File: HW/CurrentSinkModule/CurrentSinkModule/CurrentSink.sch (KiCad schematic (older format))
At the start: 103 parts, among them J1 Conn_01x03, J2 Conn_01x03, U1 LTC2058, U2 LTC2058, U3 LTC2058, U4 LTC2058

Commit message: updated
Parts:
- removed Q_NEGMOS1: IRF5210, Package_TO_SOT_THT:TO-220-3_Vertical, symbol Transistor_FET:IRF4905
- removed Q_POSMOS1: IRF3710, Package_TO_SOT_THT:TO-220-3_Vertical, symbol Transistor_FET:IRF3205
- added J3, J4: MosfetSocketx3, TerminalBlock:TerminalBlock_bornier-3_P5.08mm, symbol MosfetSocket:MosfetSocketx3
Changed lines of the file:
@@
 	1    0    0    -1
 $EndComp
-$Comp
-L Transistor_FET:IRF3205 Q_POSMOS1
-U 1 1 5C970D9A
-P 14300 4650
-F 0 "Q_POSMOS1" H 14506 4695 50  0000 L CNN
-F 1 "IRF3710" H 14506 4606 50  0000 L CNN
-F 2 "Package_TO_SOT_THT:TO-220-3_Vertical" H 14550 4575 50  0001 L CIN
-F 3 "https://www.mouser.co.uk/datasheet/2/196/irf3710pbf-1227029.pdf" H 14300 4650 50  0001 L CNN
-F 4 "942-IRF3710PBF" H 14300 4650 50  0001 C CNN "MouserNo"
-	1    14300 4650
-	1    0    0    -1
-$EndComp
-$Comp
-L Transistor_FET:IRF4905 Q_NEGMOS1
-U 1 1 5C970DA3
-P 14300 15925
-F 0 "Q_NEGMOS1" H 14506 15970 50  0000 L CNN
-F 1 "IRF5210" H 14506 15881 50  0000 L CNN
-F 2 "Package_TO_SOT_THT:TO-220-3_Vertical" H 14500 15850 50  0001 L CIN
-F 3 "https://www.mouser.co.uk/datasheet/2/196/irf5210pbf-1228304.pdf" H 14300 15925 50  0001 L CNN
-F 4 "942-IRF5210PBF" H 14300 15925 50  0001 C CNN "MouserNo"
-F 5 "942-IRF4905PBF" H 14300 15925 50  0001 C CNN "Mfr. No:"
-	1    14300 15925
-	1    0    0    1
-$EndComp
-Wire Wire Line
-	14400 3850 14400 4450
 Wire Wire Line
 	10400 4750 10400 5600
@@
 Wire Wire Line
 	5450 15400 5650 15400
-Wire Wire Line
-	14400 4850 14400 5600
 $Comp
 L Device:R R24
@@
 Wire Wire Line
 	13800 4000 13800 4650
-Wire Wire Line
-	13800 4650 14100 4650
 $Comp
 L Connector:TestPoint TP5
@@
 Connection ~ 12800 15925
 Wire Wire Line
-	12800 15925 14100 15925
+	12800 15925 14400 15925
 Wire Wire Line
 	6600 6400 7600 6400
@@
 	14400 14400 14400 15325
 Wire Wire Line
-	14400 15325 14400 15725
+	14400 15325 14400 15825
 Connection ~ 14400 15325
 Wire Wire Line
-	14400 16125 14400 17200
+	14400 16025 14400 17200
 Wire Wire Line
 	3650 20300 3650 20400
@@
 	0    1    1    0
 $EndComp
+Wire Wire Line
+	13800 4650 14400 4650
+Wire Wire Line
+	14400 4750 14400 5600
+Wire Wire Line
+	14400 3850 14400 4550
+$Comp
+L MosfetSocket:MosfetSocketx3 J3
+U 1 1 5D3BDBA1
+P 14600 4650
+F 0 "J3" H 14680 4692 50  0000 L CNN
+F 1 "MosfetSocketx3" H 14680 4601 50  0000 L CNN
+F 2 "TerminalBlock:TerminalBlock_bornier-3_P5.08mm" H 14600 4650 50  0001 C CNN
+F 3 "https://docs-emea.rs-online.com/webdocs/0130/0900766b8013040c.pdf" H 14600 4650 50  0001 C CNN
+	1    14600 4650
+	1    0    0    -1
+$EndComp
+$Comp
+L MosfetSocket:MosfetSocketx3 J4
+U 1 1 5D4094FF
+P 14600 15925
+F 0 "J4" H 14518 15600 50  0000 C CNN
+F 1 "MosfetSocketx3" H 14518 15691 50  0000 C CNN
+F 2 "TerminalBlock:TerminalBlock_bornier-3_P5.08mm" H 14600 15925 50  0001 C CNN
+F 3 "https://docs-emea.rs-online.com/webdocs/0130/0900766b8013040c.pdf" H 14600 15925 50  0001 C CNN
+	1    14600 15925
+	1    0    0    1
+$EndComp
 $EndSCHEMATC

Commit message: Updates
- New simplified current sink design: see LTSpice model "MOSFET_CurrentSense_NoSignalInversion".
Needs to be confirmed on breadboard!
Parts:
- U1, U2, U3, U4: MouserNo ADA4522-2ARZ-RL -> LTC2058
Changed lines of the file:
@@
 Connection ~ 23150 14200
-$Comp
-L Amplifier_Operational:TL072 U2
-U 1 1 5E1E06F5
-P 5700 6400
-F 0 "U2" H 5700 6767 50  0000 C CNN
-F 1 "LTC2058" H 5700 6676 50  0000 C CNN
-F 2 "Package_SO:SOIC-8_3.9x4.9mm_P1.27mm" H 5700 6400 50  0001 C CNN
-F 3 "https://www.analog.com/media/en/technical-documentation/data-sheets/ADA4522-1_4522-2_4522-4.pdf" H 5700 6400 50  0001 C CNN
-F 4 "ADA4522-2ARZ-RL" H 5700 6400 50  0001 C CNN "MouserNo"
-	1    5700 6400
-	1    0    0    -1
-$EndComp
-$Comp
-L Amplifier_Operational:TL072 U2
-U 2 1 5E1E086A
-P 8200 6500
-F 0 "U2" H 8200 6867 50  0000 C CNN
-F 1 "LTC2058" H 8200 6776 50  0000 C CNN
-F 2 "Package_SO:SOIC-8_3.9x4.9mm_P1.27mm" H 8200 6500 50  0001 C CNN
-F 3 "https://www.analog.com/media/en/technical-documentation/data-sheets/ADA4522-1_4522-2_4522-4.pdf" H 8200 6500 50  0001 C CNN
-F 4 "ADA4522-2ARZ-RL" H 8200 6500 50  0001 C CNN "MouserNo"
-	2    8200 6500
-	1    0    0    -1
-$EndComp
 $Comp
 L Amplifier_Operational:TL072 U1
@@
 F 4 "584-ADA4522-2ARMZ" H 19075 20125 50  0001 C CNN "MouserNo"
 	3    19075 20125
-	1    0    0    -1
-$EndComp
-$Comp
-L Amplifier_Operational:TL072 U1
-U 1 1 5E1E25D3
-P 5950 15300
-F 0 "U1" H 5950 15667 50  0000 C CNN
-F 1 "LTC2058" H 5950 15576 50  0000 C CNN
-F 2 "Package_SO:SOIC-8_3.9x4.9mm_P1.27mm" H 5950 15300 50  0001 C CNN
-F 3 "https://www.analog.com/media/en/technical-documentation/data-sheets/ADA4522-1_4522-2_4522-4.pdf" H 5950 15300 50  0001 C CNN
-F 4 "ADA4522-2ARZ-RL" H 5950 15300 50  0001 C CNN "MouserNo"
-	1    5950 15300
-	1    0    0    -1
-$EndComp
-$Comp
-L Amplifier_Operational:TL072 U4
-U 2 1 5E1E2914
-P 11750 15925
-F 0 "U4" H 11750 16292 50  0000 C CNN
-F 1 "LTC2058" H 11750 16201 50  0000 C CNN
-F 2 "Package_SO:SOIC-8_3.9x4.9mm_P1.27mm" H 11750 15925 50  0001 C CNN
-F 3 "https://www.analog.com/media/en/technical-documentation/data-sheets/ADA4522-1_4522-2_4522-4.pdf" H 11750 15925 50  0001 C CNN
-F 4 "ADA4522-2ARZ-RL" H 11750 15925 50  0001 C CNN "MouserNo"
-	2    11750 15925
 	1    0    0    -1
 $EndComp
@@
 Wire Wire Line
 	10300 3900 10300 6500
-$Comp
-L Amplifier_Operational:TL072 U3
-U 1 1 5D881F19
-P 12250 4650
-F 0 "U3" H 12250 5017 50  0000 C CNN
-F 1 "LTC2058" H 12250 4926 50  0000 C CNN
-F 2 "Package_SO:SOIC-8_3.9x4.9mm_P1.27mm" H 12250 4650 50  0001 C CNN
-F 3 "https://www.analog.com/media/en/technical-documentation/data-sheets/ADA4522-1_4522-2_4522-4.pdf" H 12250 4650 50  0001 C CNN
-F 4 "ADA4522-2ARZ-RL" H 12250 4650 50  0001 C CNN "MouserNo"
-	1    12250 4650
-	1    0    0    -1
-$EndComp
 Wire Wire Line
 	11950 4550 10400 4550
@@
 F 1 "LTC2058" H 24800 14576 50  0000 C CNN
 F 2 "Package_SO:SOIC-8_3.9x4.9mm_P1.27mm" H 24800 14300 50  0001 C CNN
-F 3 "https://www.analog.com/media/en/technical-documentation/data-sheets/ADA4522-1_4522-2_4522-4.pdf" H 24800 14300 50  0001 C CNN
-F 4 "ADA4522-2ARZ-RL" H 24800 14300 50  0001 C CNN "MouserNo"
+F 3 "https://www.analog.com/media/en/technical-documentation/data-sheets/LTC2058.pdf" H 24800 14300 50  0001 C CNN
+F 4 "LTC2058" H 24800 14300 50  0001 C CNN "MouserNo"
 	1    24800 14300
 	1    0    0    1
@@
 	25650 14300 25100 14300
 Connection ~ 25650 14300
-$Comp
-L Amplifier_Operational:TL072 U1
-U 2 1 5DB4E8F2
-P 7950 15400
-F 0 "U1" H 7950 15767 50  0000 C CNN
-F 1 "LTC2058" H 7950 15676 50  0000 C CNN
-F 2 "Package_SO:SOIC-8_3.9x4.9mm_P1.27mm" H 7950 15400 50  0001 C CNN
-F 3 "https://www.analog.com/media/en/technical-documentation/data-sheets/ADA4522-1_4522-2_4522-4.pdf" H 7950 15400 50  0001 C CNN
-F 4 "ADA4522-2ARZ-RL" H 7950 15400 50  0001 C CNN "MouserNo"
-	2    7950 15400
-	1    0    0    -1
-$EndComp
 Wire Wire Line
 	6800 15300 7350 15300
@@
 F 1 "LTC2058" H 24450 7526 50  0000 C CNN
 F 2 "Package_SO:SOIC-8_3.9x4.9mm_P1.27mm" H 24450 7250 50  0001 C CNN
-F 3 "https://www.analog.com/media/en/technical-documentation/data-sheets/ADA4522-1_4522-2_4522-4.pdf" H 24450 7250 50  0001 C CNN
-F 4 "ADA4522-2ARZ-RL" H 24450 7250 50  0001 C CNN "MouserNo"
+F 3 "https://www.analog.com/media/en/technical-documentation/data-sheets/LTC2058.pdf" H 24450 7250 50  0001 C CNN
+F 4 "LTC2058" H 24450 7250 50  0001 C CNN "MouserNo"
 	2    24450 7250
 	1    0    0    -1
@@
 	1    0    0    1
 $EndComp
+$Comp
+L Amplifier_Operational:TL072 U3
+U 1 1 5D881F19
+P 12250 4650
+F 0 "U3" H 12250 5017 50  0000 C CNN
+F 1 "LTC2058" H 12250 4926 50  0000 C CNN
+F 2 "Package_SO:SOIC-8_3.9x4.9mm_P1.27mm" H 12250 4650 50  0001 C CNN
+F 3 "https://www.analog.com/media/en/technical-documentation/data-sheets/LTC2058.pdf" H 12250 4650 50  0001 C CNN
+F 4 "LTC2058" H 12250 4650 50  0001 C CNN "MouserNo"
+	1    12250 4650
+	1    0    0    -1
+$EndComp
+$Comp
+L Amplifier_Operational:TL072 U2
+U 2 1 5E1E086A
+P 8200 6500
+F 0 "U2" H 8200 6867 50  0000 C CNN
+F 1 "LTC2058" H 8200 6776 50  0000 C CNN
+F 2 "Package_SO:SOIC-8_3.9x4.9mm_P1.27mm" H 8200 6500 50  0001 C CNN
+F 3 "https://www.analog.com/media/en/technical-documentation/data-sheets/LTC2058.pdf" H 8200 6500 50  0001 C CNN
+F 4 "LTC2058" H 8200 6500 50  0001 C CNN "MouserNo"
+	2    8200 6500
+	1    0    0    -1
+$EndComp
+$Comp
+L Amplifier_Operational:TL072 U2
+U 1 1 5E1E06F5
+P 5700 6400
+F 0 "U2" H 5700 6767 50  0000 C CNN
+F 1 "LTC2058" H 5700 6676 50  0000 C CNN
+F 2 "Package_SO:SOIC-8_3.9x4.9mm_P1.27mm" H 5700 6400 50  0001 C CNN
+F 3 "https://www.analog.com/media/en/technical-documentation/data-sheets/LTC2058.pdf" H 5700 6400 50  0001 C CNN
+F 4 "LTC2058" H 5700 6400 50  0001 C CNN "MouserNo"
+	1    5700 6400
+	1    0    0    -1
+$EndComp
+$Comp
+L Amplifier_Operational:TL072 U1
+U 2 1 5DB4E8F2
+P 7950 15400
+F 0 "U1" H 7950 15767 50  0000 C CNN
+F 1 "LTC2058" H 7950 15676 50  0000 C CNN
+F 2 "Package_SO:SOIC-8_3.9x4.9mm_P1.27mm" H 7950 15400 50  0001 C CNN
+F 3 "https://www.analog.com/media/en/technical-documentation/data-sheets/LTC2058.pdf" H 7950 15400 50  0001 C CNN
+F 4 "LTC2058" H 7950 15400 50  0001 C CNN "MouserNo"
+	2    7950 15400
+	1    0    0    -1
+$EndComp
+$Comp
+L Amplifier_Operational:TL072 U1
+U 1 1 5E1E25D3
+P 5950 15300
+F 0 "U1" H 5950 15667 50  0000 C CNN
+F 1 "LTC2058" H 5950 15576 50  0000 C CNN
+F 2 "Package_SO:SOIC-8_3.9x4.9mm_P1.27mm" H 5950 15300 50  0001 C CNN
+F 3 "https://www.analog.com/media/en/technical-documentation/data-sheets/LTC2058.pdf" H 5950 15300 50  0001 C CNN
+F 4 "LTC2058" H 5950 15300 50  0001 C CNN "MouserNo"
+	1    5950 15300
+	1    0    0    -1
+$EndComp
+$Comp
+L Amplifier_Operational:TL072 U4
+U 2 1 5E1E2914
+P 11750 15925
+F 0 "U4" H 11750 16292 50  0000 C CNN
+F 1 "LTC2058" H 11750 16201 50  0000 C CNN
+F 2 "Package_SO:SOIC-8_3.9x4.9mm_P1.27mm" H 11750 15925 50  0001 C CNN
+F 3 "https://www.analog.com/media/en/technical-documentation/data-sheets/LTC2058.pdf" H 11750 15925 50  0001 C CNN
+F 4 "LTC2058" H 11750 15925 50  0001 C CNN "MouserNo"
+	2    11750 15925
+	1    0    0    -1
+$EndComp
 $EndSCHEMATC

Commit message: updated
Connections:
- net GNDS: now also R5.1; no longer R8.1
- net at C3.1, JP5.2, R19.1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: now also R7.1; no longer JP7.1, U1.5 (+)
- net at C4.1, JP6.2, R20.1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: now also R25.1; no longer JP8.1, U2.5 (+)
- net at J2.1 (Pin_1), JP8.2, U2.7: now also R6.1; no longer R25.2
- net at R6.2, U2.6 (-): now also JP8.1
- net at J1.1 (Pin_1), R8.2: now also JP7.2, U1.7; no longer R5.1, R7.1
- net at R5.2: now also U1.5 (+); no longer U1.6 (-)
- net +5V renamed +12V
- net +5VA renamed +12VA
- net -5V renamed -12V
- net -5VA renamed -12VA
- new net: R25.2, R26.2, U2.5 (+)
- new net: JP7.1, R7.2, R8.1, U1.6 (-)
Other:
- moved on the sheet: JP7, JP8, R23, R25, R26, R5, R6, R7, R8, U1B, U2B

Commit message: Finished CurrentSinkRevC layout
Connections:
- net +12VA is gone; now on net +12V: C21.2, C25.1, C31.1, C33.1, C5.1, C7.1, U1.8 (V+), U4.8 (V+), U_NEGIA1.7 (Vs+)
- net -12VA is gone; now on net -12V: C22.2, C26.1, C32.1, C34.1, C6.1, C8.1, U1.4 (V-), U4.4 (V-), U_NEGIA1.4 (Vs-)
- net ADCSIG2: now also U4.7; no longer U4.1
- net at J4.1 (Pin_1), TP5.1: now also U4.1; no longer U4.7
- net at R21.2: now also U4.2 (-); no longer U4.5 (+)
- net at R22.1: now also U4.5 (+); no longer U4.3 (+)
- net at R13.1, R16.1: now also U4.6 (-); no longer U4.2 (-)
- net at J1.2 (Pin_2): now also U4.3 (+); no longer U4.6 (-)
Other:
- moved on the sheet: U4A, U4B

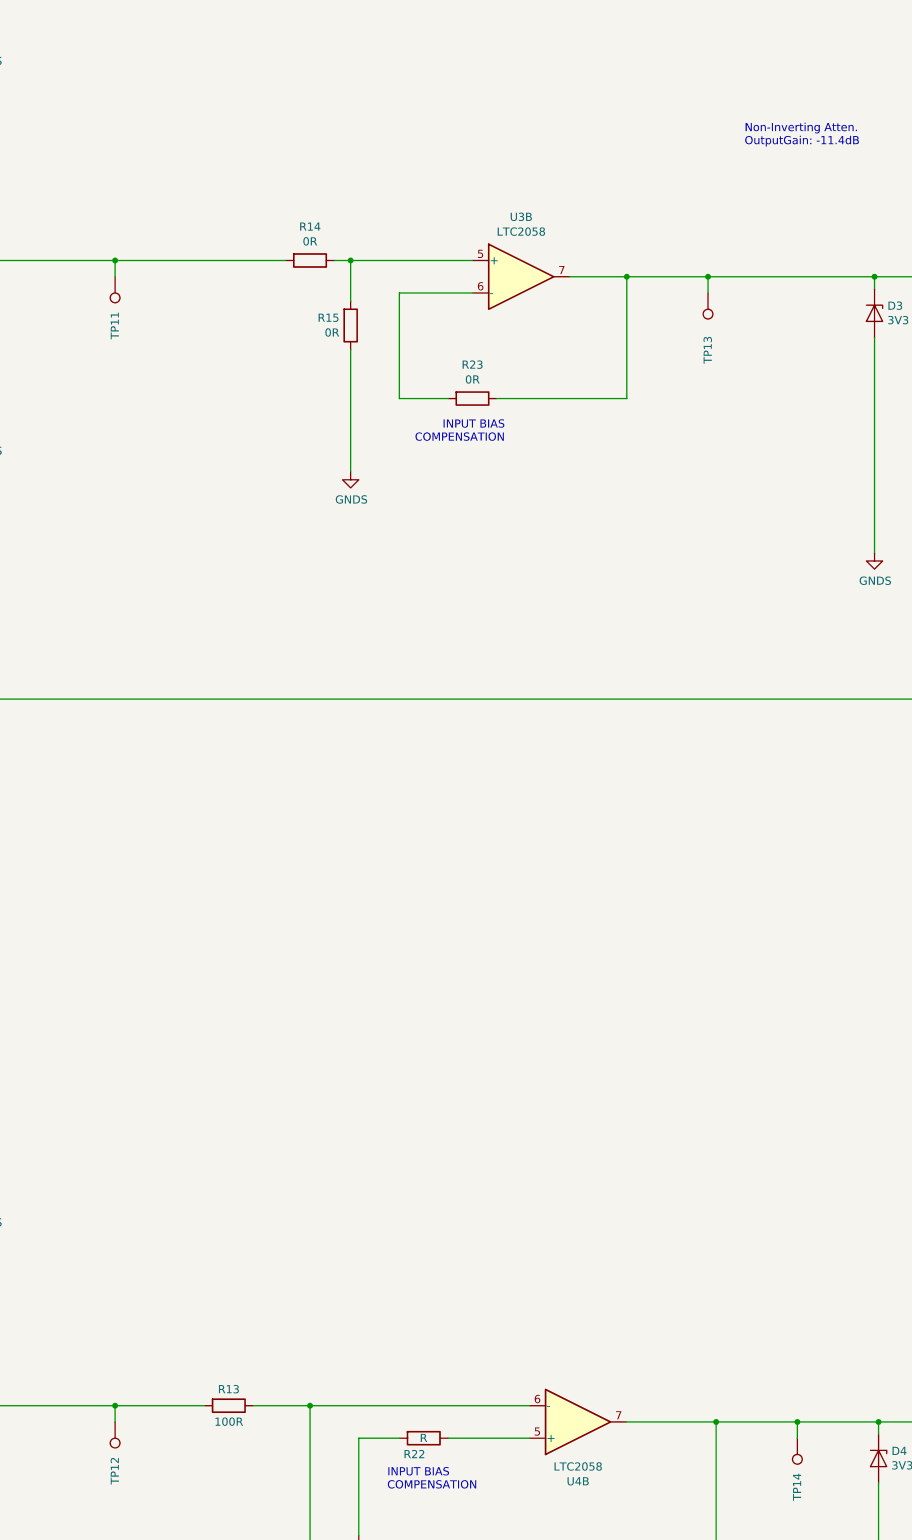
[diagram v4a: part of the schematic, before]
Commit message: Added Interafec IBOMS
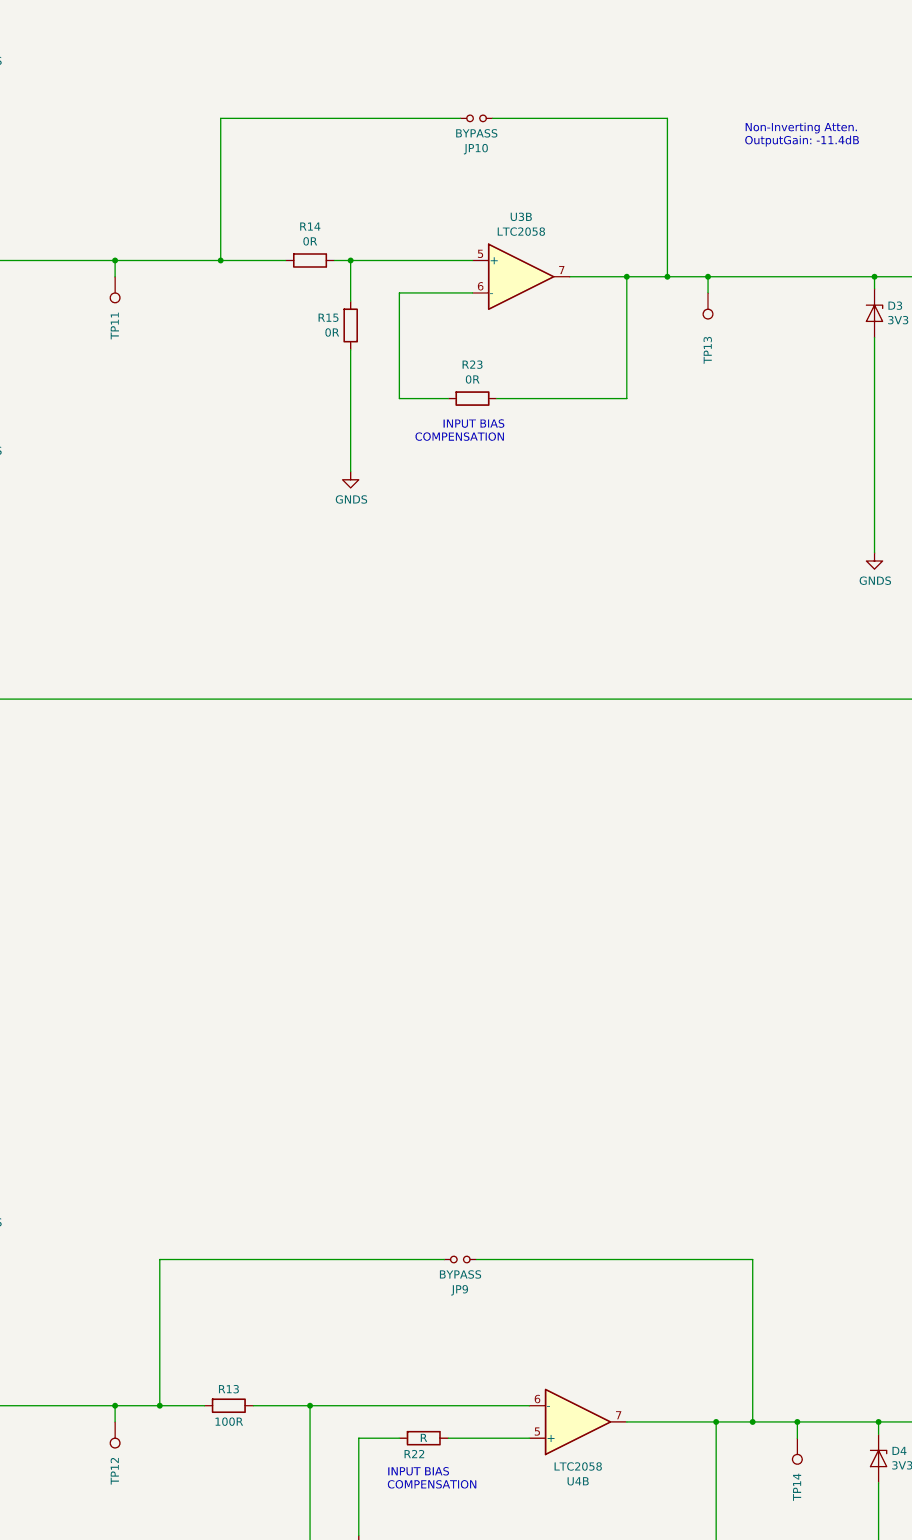
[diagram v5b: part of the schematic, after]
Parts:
- added JP10, JP9: BYPASS, Jumper:SolderJumper-2_P1.3mm_Open_Pad1.0x1.5mm, symbol Device:Jumper_NO_Small
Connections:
- net ADCSIG1: now also JP10.2
- net ADCSIG2: now also JP9.2
- net at R14.2, TP11.1, U_POSIA1.6: now also JP10.1
- net at R13.2, TP12.1, U_NEGIA1.6: now also JP9.1
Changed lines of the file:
@@
 	25100 8000 25100 7250
 Wire Wire Line
-	25100 7250 25600 7250
+	25100 7250 25350 7250
 $Comp
 L Device:R R14
@@
 $EndComp
 Wire Wire Line
-	23000 7150 21950 7150
+	23000 7150 22600 7150
 Connection ~ 21950 7150
 Wire Wire Line
@@
 $EndComp
 Wire Wire Line
-	21950 14200 22500 14200
+	21950 14200 22225 14200
 Connection ~ 21950 14200
 Wire Wire Line
@@
 ADCSIG2
 Wire Wire Line
-	25650 14300 26150 14300
+	25650 14300 25875 14300
 Wire Wire Line
 	25650 14300 25100 14300
@@
 	-1   0    0    1
 $EndComp
+$Comp
+L Device:Jumper_NO_Small JP10
+U 1 1 5D36180C
+P 24175 6275
+F 0 "JP10" H 24175 6460 50  0000 C CNN
+F 1 "BYPASS" H 24175 6369 50  0000 C CNN
+F 2 "Jumper:SolderJumper-2_P1.3mm_Open_Pad1.0x1.5mm" H 24175 6275 50  0001 C CNN
+F 3 "~" H 24175 6275 50  0001 C CNN
+	1    24175 6275
+	1    0    0    1
+$EndComp
+Wire Wire Line
+	24075 6275 22600 6275
+Wire Wire Line
+	22600 6275 22600 7150
+Connection ~ 22600 7150
+Wire Wire Line
+	22600 7150 21950 7150
+Wire Wire Line
+	24275 6275 25350 6275
+Wire Wire Line
+	25350 6275 25350 7250
+Connection ~ 25350 7250
+Wire Wire Line
+	25350 7250 25600 7250
+$Comp
+L Device:Jumper_NO_Small JP9
+U 1 1 5D3A9422
+P 24075 13300
+F 0 "JP9" H 24075 13485 50  0000 C CNN
+F 1 "BYPASS" H 24075 13394 50  0000 C CNN
+F 2 "Jumper:SolderJumper-2_P1.3mm_Open_Pad1.0x1.5mm" H 24075 13300 50  0001 C CNN
+F 3 "~" H 24075 13300 50  0001 C CNN
+	1    24075 13300
+	1    0    0    1
+$EndComp
+Wire Wire Line
+	23975 13300 22225 13300
+Wire Wire Line
+	22225 13300 22225 14200
+Connection ~ 22225 14200
+Wire Wire Line
+	22225 14200 22500 14200
+Wire Wire Line
+	24175 13300 25875 13300
+Wire Wire Line
+	25875 13300 25875 14300
+Connection ~ 25875 14300
+Wire Wire Line
+	25875 14300 26150 14300
 $EndSCHEMATC
